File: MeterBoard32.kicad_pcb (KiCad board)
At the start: 2 copper layers, 49 x 63.3 mm, 38 parts, among them J1 Screw_Terminal_01x02, M1 MICRO_USB_18_TH, Q1 S8050, Q2 S8050, U1 AMS1117-3V3, U2 CP2102N-GQFN24, U3 ESP32-WROOM, U5 TSS721A

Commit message: Small fix
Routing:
- added copper zone on B.Cu, net GND
- added copper zone on F.Cu, net GND
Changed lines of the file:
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@@
   (via (at 108.1 84.8) (size 0.6) (drill 0.4) (layers F.Cu B.Cu) (net 2))
   (segment (start 107.06235 83.76235) (end 108.1 84.8) (width 0.25) (layer F.Cu) (net 2))
-  (segment (start 119.3744 74.2753) (end 115.925 77.7247) (width 0.25) (layer F.Cu) (net 2))
-  (segment (start 119.875 74.2753) (end 119.3744 74.2753) (width 0.25) (layer F.Cu) (net 2))
   (segment (start 119.875 73.2) (end 119.875 74.2753) (width 0.25) (layer F.Cu) (net 2))
   (segment (start 115.925 79.4) (end 115.925 79.15) (width 0.25) (layer F.Cu) (net 2))
@@
   (segment (start 102.15 44.935) (end 102.15 41.196) (width 0.25) (layer F.Cu) (net 2))
   (segment (start 96.735 51.15) (end 96.735 50.35) (width 0.25) (layer F.Cu) (net 2))
+  (segment (start 119.3744 74.2753) (end 115.925 77.7247) (width 0.25) (layer F.Cu) (net 2))
+  (segment (start 119.875 74.2753) (end 119.3744 74.2753) (width 0.25) (layer F.Cu) (net 2))
   (segment (start 84.1625 48.26) (end 84.45 47.9725) (width 0.25) (layer F.Cu) (net 3))
   (segment (start 84.45 47.9725) (end 83.5325 47.9725) (width 0.25) (layer F.Cu) (net 3))
@@
   (via (at 118.11 54.60999) (size 0.6) (drill 0.4) (layers F.Cu B.Cu) (net 75))
   (segment (start 123.19 52.07) (end 120.65001 54.60999) (width 0.25) (layer B.Cu) (net 75))
+  (zone (net 2) (net_name GND) (layer F.Cu) (hatch edge 0.508)
+    (connect_pads (clearance 0.508))
+    (min_thickness 0.254)
+    (fill yes (arc_segments 32) (thermal_gap 0.508) (thermal_bridge_width 0.508))
+    (polygon
+      (pts
+        (xy 126.86873 94.534859) (xy 77.98975 94.534859) (xy 77.98975 31.543983) (xy 78.039746 31.493987) (xy 126.86873 31.493987)
+      )
+    )
+    (polygon
+      (pts
+        (xy 78.039746 31.493987) (xy 77.989877 31.493987) (xy 78.013218 31.517328) (xy 77.98975 31.517328) (xy 77.98975 31.493987)
+        (xy 77.989877 31.493987) (xy 77.98975 31.49386) (xy 78.039873 31.49386)
+      )
+    )
+  )
+  (zone (net 2) (net_name GND) (layer B.Cu) (hatch edge 0.508)
+    (connect_pads (clearance 0.508))
+    (min_thickness 0.254)
+    (fill yes (arc_segments 32) (thermal_gap 0.508) (thermal_bridge_width 0.508))
+    (polygon
+      (pts
+        (xy 127 93.98) (xy 127 94.531007) (xy 77.940469 94.531007) (xy 77.940469 31.75) (xy 126.602539 31.75)
+      )
+    )
+  )
 )

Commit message: Small fixes again..
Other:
- board text added: "Rev. 2"
- board text removed: "Rev. 1"
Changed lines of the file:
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@@
     (effects (font (size 1.5 1.5) (thickness 0.3)) (justify mirror))
   )
-  (gr_text "Rev. 1" (at 85.5 82.9) (layer F.SilkS)
+  (gr_text "Rev. 2" (at 85.5 82.9) (layer F.SilkS)
     (effects (font (size 1.5 1.5) (thickness 0.3)))
   )

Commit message: Fixed 3D models
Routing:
- net /EN: track 59.9 -> 54.2 mm
- net +3V3: track 141.2 -> 142.1 mm

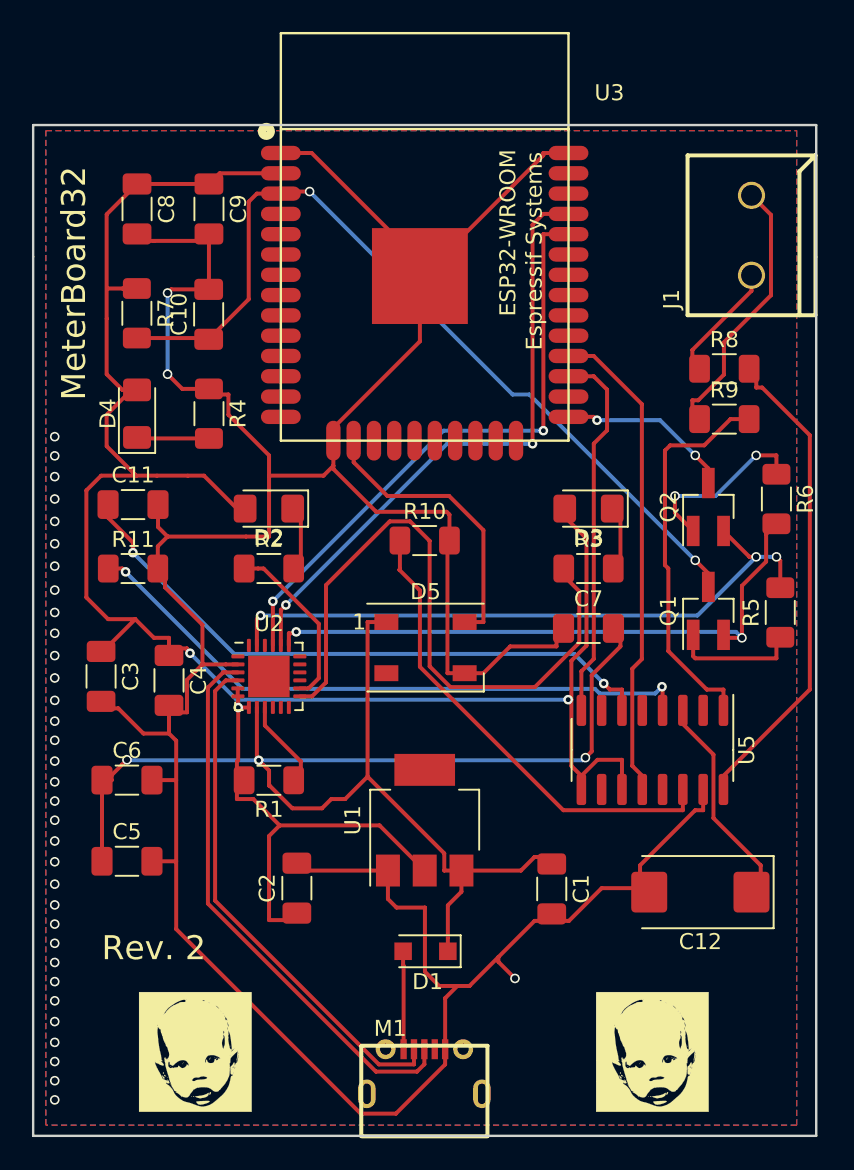
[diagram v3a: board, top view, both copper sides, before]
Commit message: Finished the conversion of MeterBoard32 from KiCad 4 to KiCad 5
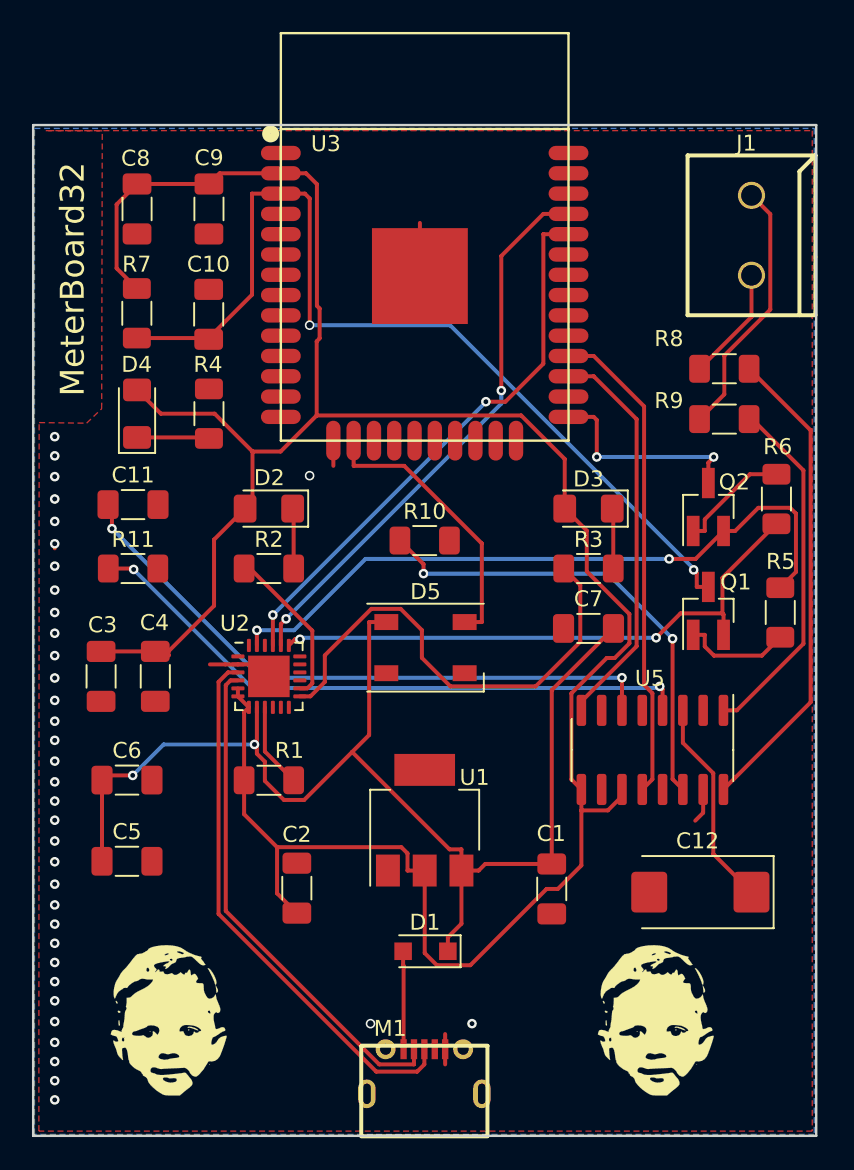
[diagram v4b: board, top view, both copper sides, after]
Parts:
- removed G2: LOGO, Harry:Harry
- added G1: LOGO, Harry:Harry_3, F.Cu at (116.8, 87.6)
- G1: footprint Harry:Harry -> Harry:Harry_3
- moved G1 2.48 mm to (86.4, 87.6)
- moved C4 0.89 mm to (85.6, 65.9)
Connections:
- U2 pad 25: (no net) -> GND
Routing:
- net GND: track 216.3 -> 13.6 mm
- net +3V3: track 142.1 -> 160.3 mm, vias 3 -> 0
- net VBUS: track 89.1 -> 75.6 mm, vias 3 -> 2
- net /LED_RX: track 40.9 -> 30.0 mm
- net Net-(Q2-Pad1): track 11.6 -> 7.11 mm, vias 2 -> 0
- net /EN: track 54.2 -> 58.7 mm
- net /MCU_TX: track 38.5 -> 35.4 mm
- net /MCU_RX: track 38.0 -> 35.0 mm
- net /DTR: track 40.4 -> 43.0 mm, vias 3 -> 2
- net /BUS_2: track 24.7 -> 22.3 mm
- net /IO0: track 11.0 -> 13.2 mm
- net /RTS: track 38.6 -> 36.3 mm
- net /UART_RX: track 23.3 -> 25.0 mm
- net /LED_TX: track 11.4 -> 10.1 mm
- net Net-(Q1-Pad1): track 8.02 -> 6.89 mm
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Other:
- board text removed: "Rev. 2"
